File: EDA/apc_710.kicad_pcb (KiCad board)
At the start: 2 copper layers, 218 x 42 mm, 49 parts

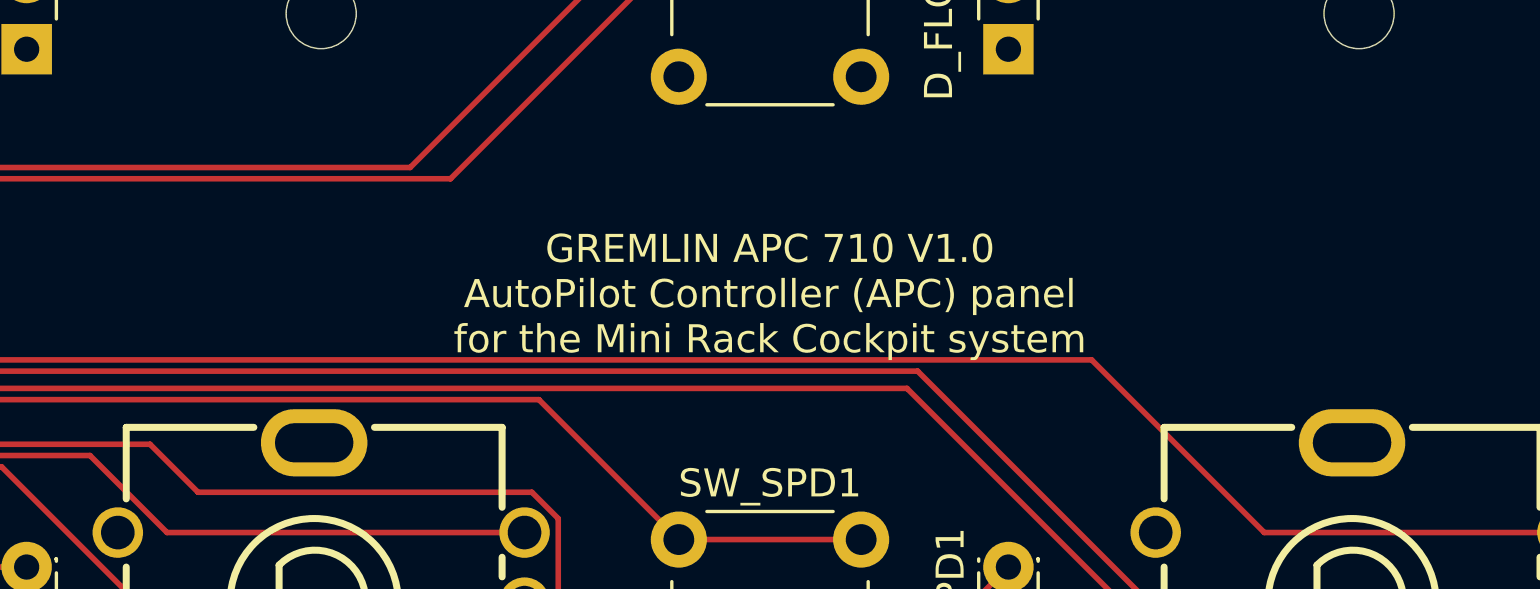
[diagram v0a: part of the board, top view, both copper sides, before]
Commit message: GitHub info
* added exception for schematic lockfiles
* added github link to readme
* added github link to pcb, pcb diagram, and schematic diagram
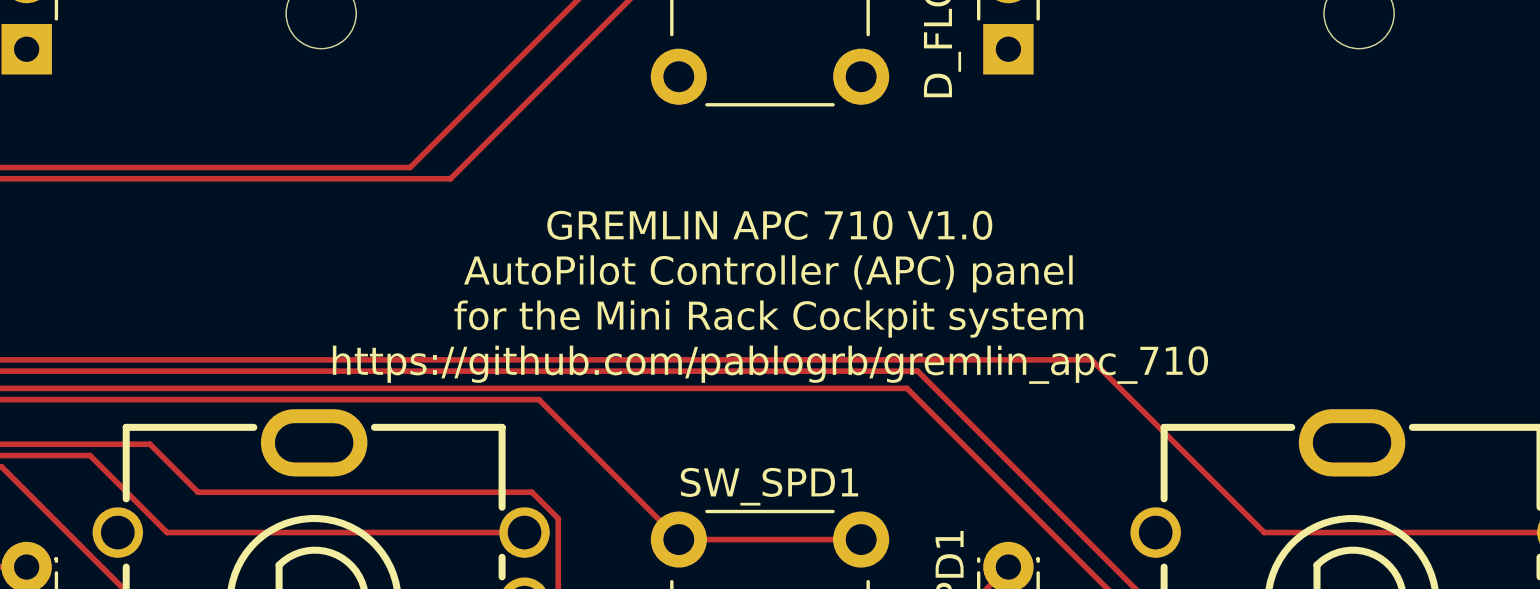
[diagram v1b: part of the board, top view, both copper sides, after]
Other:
- board text added: "GREMLIN APC 710 V1.0 AutoPilot Controller (APC) panel for the Mini Rack Cockpit system https://github.com/pablogrb/gremlin_apc_710"
- board text removed: "GREMLIN APC 710 V1.0 AutoPilot Controller (APC) panel for the Mini Rack Cockpit system"
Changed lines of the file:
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@@
 		(date "2026-03-31")
 		(rev "V1.0")
-		(comment 1 "https://creativecommons.org/licenses/by-nc/3.0/")
-		(comment 2 "Creative Commons Attribution-NonCommercial 3.0")
+		(comment 1 "https://github.com/pablogrb/gremlin_apc_710")
+		(comment 2 "https://creativecommons.org/licenses/by-nc/3.0/")
+		(comment 3 "Creative Commons Attribution-NonCommercial 3.0")
 	)
 	(layers
@@
 		(layer "F.CrtYd")
 	)
-	(gr_text "GREMLIN APC 710 V1.0\nAutoPilot Controller (APC) panel\nfor the Mini Rack Cockpit system"
+	(gr_text "GREMLIN APC 710 V1.0\nAutoPilot Controller (APC) panel\nfor the Mini Rack Cockpit system\nhttps://github.com/pablogrb/gremlin_apc_710"
 		(at 285 145.5 0)
 		(layer "F.SilkS")
@@
 		)
 	)
-	(gr_text "GREMLIN APC 710 V1.0\nAutoPilot Controller (APC) panel\nfor the Mini Rack Cockpit system"
+	(gr_text "GREMLIN APC 710 V1.0\nAutoPilot Controller (APC) panel\nfor the Mini Rack Cockpit system\nhttps://github.com/pablogrb/gremlin_apc_710"
 		(at 285 145.5 0)
 		(layer "B.SilkS")
